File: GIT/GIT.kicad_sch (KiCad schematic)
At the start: 2 parts

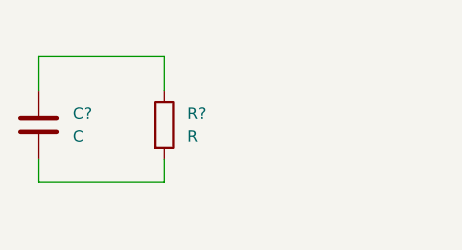
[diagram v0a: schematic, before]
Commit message: added new resitor and annotated
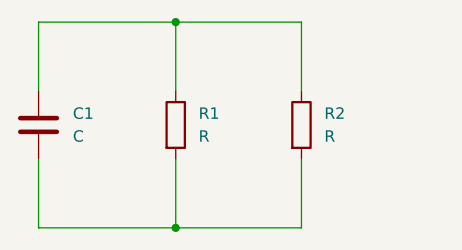
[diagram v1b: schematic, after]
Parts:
- added R2: R, symbol Device:R
- gave numbers to parts that had none: 2
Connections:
- net at C1.1, R1.1: now also R2.1
- net at C1.2, R1.2: now also R2.2
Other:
- moved on the sheet: R1
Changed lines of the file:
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@@
 	(generator_version "8.0")
 	(paper "A4")
-	(wire
-		(pts
-			(xy 133.35 83.82) (xy 133.35 87.63)
-		)
-		(stroke
-			(width 0)
-			(type default)
-		)
-	)
-	(wire
-		(pts
-			(xy 133.35 97.79) (xy 133.35 95.25)
-		)
-		(stroke
-			(width 0)
-			(type default)
-		)
-	)
-	(wire
-		(pts
-			(xy 147.32 83.82) (xy 147.32 87.63)
-		)
-		(stroke
-			(width 0)
-			(type default)
-		)
-	)
-	(wire
-		(pts
-			(xy 133.35 83.82) (xy 147.32 83.82)
-		)
-		(stroke
-			(width 0)
-			(type default)
-		)
-	)
-	(wire
-		(pts
-			(xy 147.32 97.79) (xy 147.32 95.25)
-		)
-		(stroke
-			(width 0)
-			(type default)
-		)
-	)
-	(wire
-		(pts
-			(xy 133.35 97.79) (xy 147.32 97.79)
+	(junction
+		(at 148.59 102.87)
+		(diameter 0)
+		(color 0 0 0 0)
+	)
+	(junction
+		(at 148.59 80.01)
+		(diameter 0)
+		(color 0 0 0 0)
+	)
+	(wire
+		(pts
+			(xy 133.35 80.01) (xy 133.35 87.63)
+		)
+		(stroke
+			(width 0)
+			(type default)
+		)
+	)
+	(wire
+		(pts
+			(xy 133.35 102.87) (xy 133.35 95.25)
+		)
+		(stroke
+			(width 0)
+			(type default)
+		)
+	)
+	(wire
+		(pts
+			(xy 148.59 80.01) (xy 148.59 87.63)
+		)
+		(stroke
+			(width 0)
+			(type default)
+		)
+	)
+	(wire
+		(pts
+			(xy 133.35 80.01) (xy 148.59 80.01)
+		)
+		(stroke
+			(width 0)
+			(type default)
+		)
+	)
+	(wire
+		(pts
+			(xy 162.56 80.01) (xy 148.59 80.01)
+		)
+		(stroke
+			(width 0)
+			(type default)
+		)
+	)
+	(wire
+		(pts
+			(xy 162.56 102.87) (xy 148.59 102.87)
+		)
+		(stroke
+			(width 0)
+			(type default)
+		)
+	)
+	(wire
+		(pts
+			(xy 148.59 102.87) (xy 148.59 95.25)
+		)
+		(stroke
+			(width 0)
+			(type default)
+		)
+	)
+	(wire
+		(pts
+			(xy 162.56 95.25) (xy 162.56 102.87)
+		)
+		(stroke
+			(width 0)
+			(type default)
+		)
+	)
+	(wire
+		(pts
+			(xy 162.56 87.63) (xy 162.56 80.01)
+		)
+		(stroke
+			(width 0)
+			(type default)
+		)
+	)
+	(wire
+		(pts
+			(xy 133.35 102.87) (xy 148.59 102.87)
 		)
 		(stroke
@@
 		(dnp no)
 		(fields_autoplaced yes)
-		(property "Reference" "C?"
+		(property "Reference" "C1"
 			(at 137.16 90.1699 0)
 			(effects
@@
 			(project ""
 				(path "/cc2011f6-6135-4ac0-8f43-1e17b35da812"
-					(reference "C?")
+					(reference "C1")
 					(unit 1)
 				)
@@
 	(symbol
 		(lib_id "Device:R")
-		(at 147.32 91.44 0)
+		(at 148.59 91.44 0)
 		(unit 1)
 		(exclude_from_sim no)
@@
 		(dnp no)
 		(fields_autoplaced yes)
-		(property "Reference" "R?"
-			(at 149.86 90.1699 0)
+		(property "Reference" "R1"
+			(at 151.13 90.1699 0)
 			(effects
 				(font
@@
 		)
 		(property "Value" "R"
-			(at 149.86 92.7099 0)
+			(at 151.13 92.7099 0)
 			(effects
 				(font
@@
 		)
 		(property "Footprint" ""
-			(at 145.542 91.44 90)
+			(at 146.812 91.44 90)
 			(effects
 				(font
@@
 		)
 		(property "Datasheet" "~"
-			(at 147.32 91.44 0)
+			(at 148.59 91.44 0)
 			(effects
 				(font
@@
 		)
 		(property "Description" "Resistor"
-			(at 147.32 91.44 0)
+			(at 148.59 91.44 0)
 			(effects
 				(font
@@
 			(project ""
 				(path "/cc2011f6-6135-4ac0-8f43-1e17b35da812"
-					(reference "R?")
+					(reference "R1")
 					(unit 1)
 				)
+			)
+		)
+	)
+	(symbol
+		(lib_id "Device:R")
+		(at 162.56 91.44 0)
+		(unit 1)
+		(exclude_from_sim no)
+		(in_bom yes)
+		(on_board yes)
+		(dnp no)
+		(fields_autoplaced yes)
+		(property "Reference" "R2"
+			(at 165.1 90.1699 0)
+			(effects
+				(font
+					(size 1.27 1.27)
+				)
+				(justify left)
+			)
+		)
+		(property "Value" "R"
+			(at 165.1 92.7099 0)
+			(effects
+				(font
+					(size 1.27 1.27)
+				)
+				(justify left)
+			)
+		)
+		(property "Footprint" ""
+			(at 160.782 91.44 90)
+			(effects
+				(font
+					(size 1.27 1.27)
+				)
+				(hide yes)
+			)
+		)
+		(property "Datasheet" "~"
+			(at 162.56 91.44 0)
+			(effects
+				(font
+					(size 1.27 1.27)
+				)
+				(hide yes)
+			)
+		)
+		(property "Description" "Resistor"
+			(at 162.56 91.44 0)
+			(effects
+				(font
+					(size 1.27 1.27)
+				)
+				(hide yes)
+			)
+		)
+		(pin "2"
+		)
+		(pin "1"
+		)
+		(instances
+			(project "GIT"
+				(path "/cc2011f6-6135-4ac0-8f43-1e17b35da812"
+					(reference "R2")
+					(unit 1)
+				)

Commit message: added one R
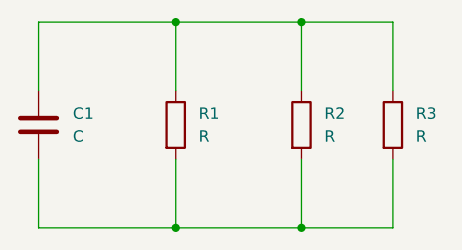
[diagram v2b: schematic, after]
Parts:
- added R3: R, symbol Device:R
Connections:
- net at C1.1, R1.1, R2.1: now also R3.1
- net at C1.2, R1.2, R2.2: now also R3.2
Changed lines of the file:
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@@
 	(paper "A4")
+	(junction
+		(at 162.56 102.87)
+		(diameter 0)
+		(color 0 0 0 0)
+	)
+	(junction
+		(at 162.56 80.01)
+		(diameter 0)
+		(color 0 0 0 0)
+	)
 	(junction
 		(at 148.59 102.87)
@@
 	(wire
 		(pts
+			(xy 162.56 102.87) (xy 172.72 102.87)
+		)
+		(stroke
+			(width 0)
+			(type default)
+		)
+	)
+	(wire
+		(pts
+			(xy 172.72 80.01) (xy 162.56 80.01)
+		)
+		(stroke
+			(width 0)
+			(type default)
+		)
+	)
+	(wire
+		(pts
 			(xy 133.35 102.87) (xy 133.35 95.25)
 		)
@@
 	(wire
 		(pts
+			(xy 172.72 95.25) (xy 172.72 102.87)
+		)
+		(stroke
+			(width 0)
+			(type default)
+		)
+	)
+	(wire
+		(pts
+			(xy 172.72 87.63) (xy 172.72 80.01)
+		)
+		(stroke
+			(width 0)
+			(type default)
+		)
+	)
+	(wire
+		(pts
 			(xy 162.56 80.01) (xy 148.59 80.01)
 		)
@@
 	(wire
 		(pts
-			(xy 162.56 102.87) (xy 148.59 102.87)
+			(xy 148.59 102.87) (xy 162.56 102.87)
 		)
 		(stroke
@@
 					(unit 1)
 				)
+			)
+		)
+	)
+	(symbol
+		(lib_id "Device:R")
+		(at 172.72 91.44 0)
+		(unit 1)
+		(exclude_from_sim no)
+		(in_bom yes)
+		(on_board yes)
+		(dnp no)
+		(fields_autoplaced yes)
+		(property "Reference" "R3"
+			(at 175.26 90.1699 0)
+			(effects
+				(font
+					(size 1.27 1.27)
+				)
+				(justify left)
+			)
+		)
+		(property "Value" "R"
+			(at 175.26 92.7099 0)
+			(effects
+				(font
+					(size 1.27 1.27)
+				)
+				(justify left)
+			)
+		)
+		(property "Footprint" ""
+			(at 170.942 91.44 90)
+			(effects
+				(font
+					(size 1.27 1.27)
+				)
+				(hide yes)
+			)
+		)
+		(property "Datasheet" "~"
+			(at 172.72 91.44 0)
+			(effects
+				(font
+					(size 1.27 1.27)
+				)
+				(hide yes)
+			)
+		)
+		(property "Description" "Resistor"
+			(at 172.72 91.44 0)
+			(effects
+				(font
+					(size 1.27 1.27)
+				)
+				(hide yes)
+			)
+		)
+		(pin "2"
+		)
+		(pin "1"
+		)
+		(instances
+			(project "GIT"
+				(path "/cc2011f6-6135-4ac0-8f43-1e17b35da812"
+					(reference "R3")
+					(unit 1)
+				)
